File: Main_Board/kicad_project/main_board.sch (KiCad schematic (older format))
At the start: 0 parts

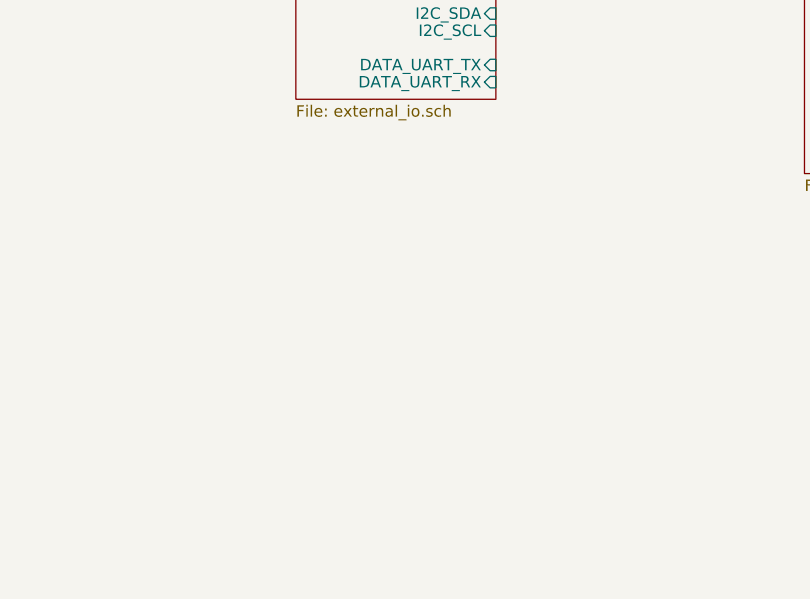
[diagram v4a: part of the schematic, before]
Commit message: MCU pinout done
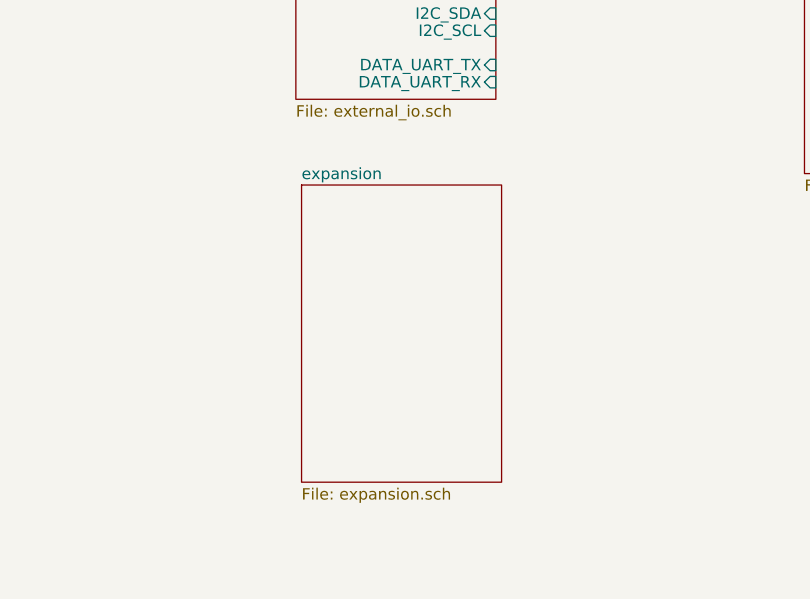
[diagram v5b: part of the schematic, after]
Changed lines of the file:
@@
 $Descr A4 11693 8268
 encoding utf-8
-Sheet 1 9
+Sheet 1 10
 Title "Cube Main Board - top level schematic"
 Date ""
@@
 Wire Bus Line
 	4475 2875 5225 2875
+$Sheet
+S 3025 4625 875  1300
+U 5FDB67B7
+F0 "expansion" 50
+F1 "expansion.sch" 50
+$EndSheet
 $EndSCHEMATC

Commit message: schematic rev1 finished
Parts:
- added R70: 1K, Resistor_SMD:R_0603_1608Metric, symbol Device:R_Small
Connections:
- new net MCU/STEP_UART_RX: R70.2
- new net MCU/STEP_UART_TX: R70.1
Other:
- note added: "Cube Main Board V2"
- note added: "Top level schematic"

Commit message: routing half finished
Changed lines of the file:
@@
 F2 "3V3" I R 4000 3300 50
 F3 "12V" I R 4000 3150 50
-F4 "USB_DP" I R 4000 3450 50
-F5 "USB_DM" I R 4000 3525 50
+F4 "USB_DATA_P" I R 4000 3450 50
+F5 "USB_DATA_N" I R 4000 3525 50
 F6 "I2C_SDA" I R 4000 3675 50
 F7 "I2C_SCL" I R 4000 3750 50
